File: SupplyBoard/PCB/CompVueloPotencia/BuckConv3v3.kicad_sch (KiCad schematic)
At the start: 11 parts, among them U1 TPS5430DDA

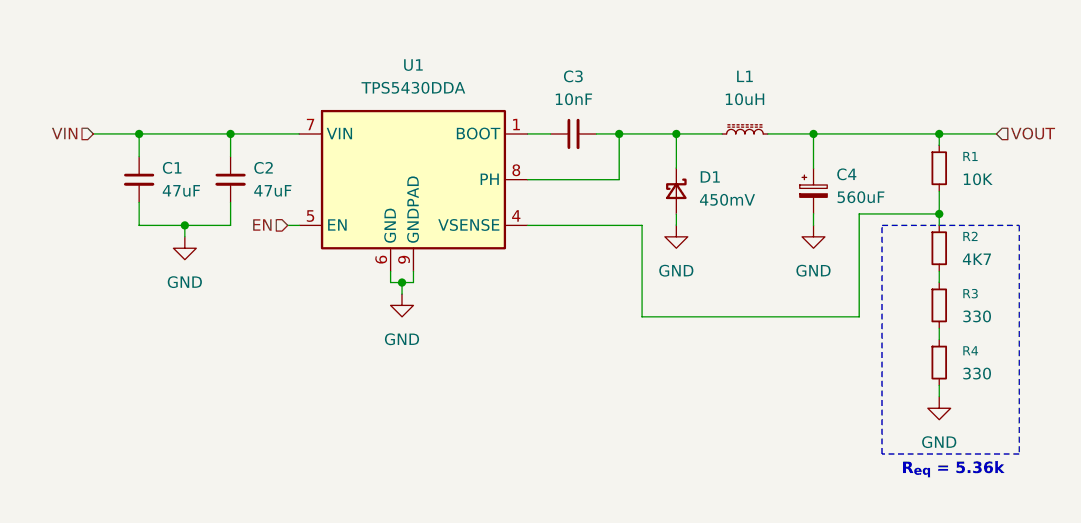
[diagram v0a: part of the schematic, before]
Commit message: SupplyBoard - finish current sense
Finish the Current Sensor Circuit and add more 3.3V out, i change de microcontroles to a mcu that have the exact GPIO's
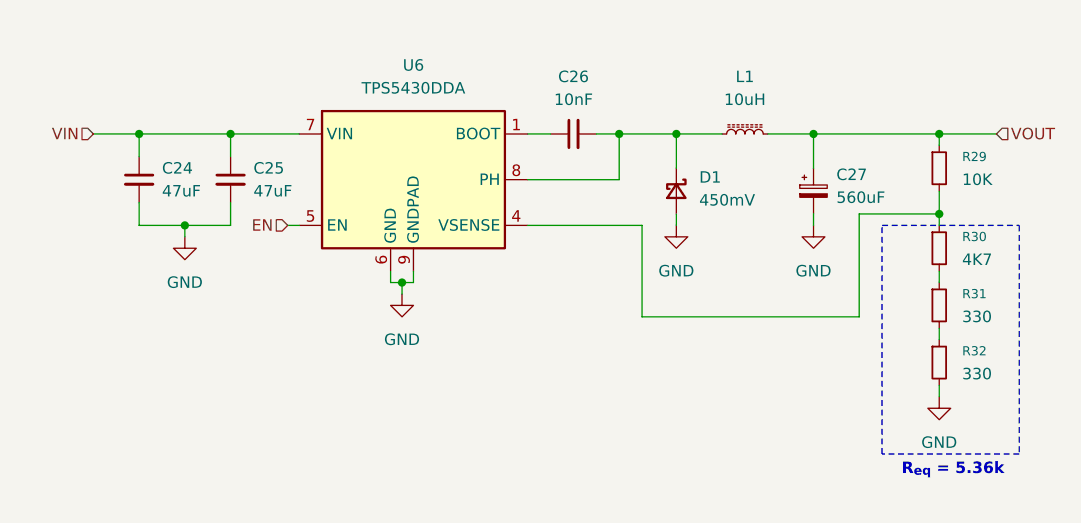
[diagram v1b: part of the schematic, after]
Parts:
- renumbered C1 to C24, C2 to C25, C3 to C26, C4 to C27, R1 to R29, R2 to R30, R3 to R31, R4 to R32, U1 to U6

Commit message: SupplyBoard - update layout
schematic completed and PCB layout started; only the routing of the traces remains to be done
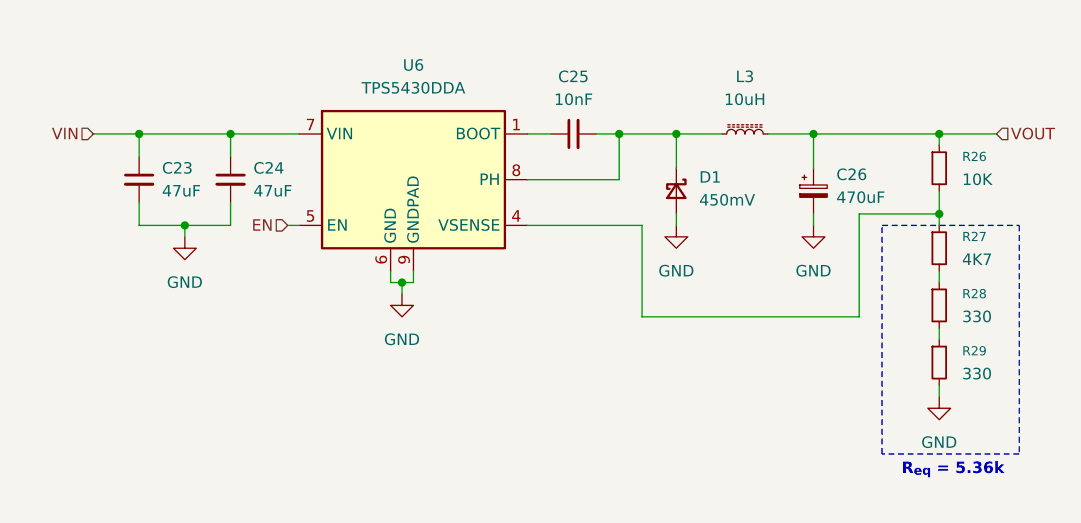
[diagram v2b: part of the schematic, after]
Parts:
- C23: renamed from C24; footprint (none) -> Capacitor_SMD:C_0805_2012Metric_Pad1.18x1.45mm_HandSolder
- C24: renamed from C25; footprint (none) -> Capacitor_SMD:C_0805_2012Metric_Pad1.18x1.45mm_HandSolder
- C25: renamed from C26; footprint (none) -> Capacitor_SMD:C_0805_2012Metric_Pad1.18x1.45mm_HandSolder
- C26: renamed from C27; value 560uF -> 470uF; footprint (none) -> Capacitor_Tantalum_SMD:CP_EIA-7343-31_Kemet-D_HandSolder
- D1: footprint (none) -> Diode_SMD:D_SMA-SMB_Universal_Handsoldering
- L3: renamed from L1; footprint (none) -> Inductor_SMD:L_Bourns_SRN6045TA
- R26: renamed from R29; footprint (none) -> Resistor_SMD:R_0805_2012Metric_Pad1.20x1.40mm_HandSolder
- R27: renamed from R30; footprint (none) -> Resistor_SMD:R_0805_2012Metric_Pad1.20x1.40mm_HandSolder
- R28: renamed from R31; footprint (none) -> Resistor_SMD:R_0805_2012Metric_Pad1.20x1.40mm_HandSolder
- R29: renamed from R32; footprint (none) -> Resistor_SMD:R_0805_2012Metric_Pad1.20x1.40mm_HandSolder
- U6: footprint Package_SO:TI_SO-PowerPAD-8_ThermalVias -> CompVuelo:Texas_S-PDSO-G8_3x3mm_P0.65mm
